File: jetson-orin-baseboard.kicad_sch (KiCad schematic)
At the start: 4 parts

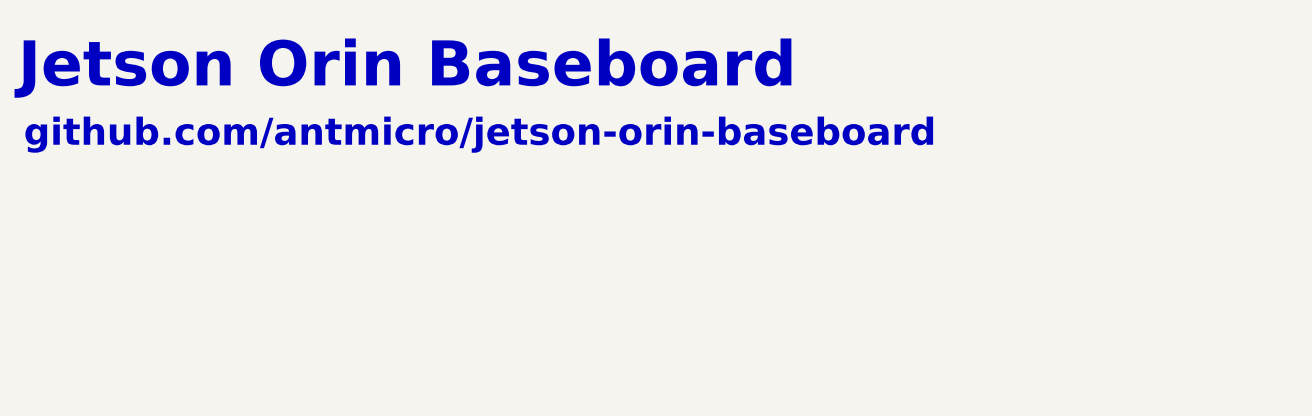
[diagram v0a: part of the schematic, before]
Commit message: PCIE Simplification finished
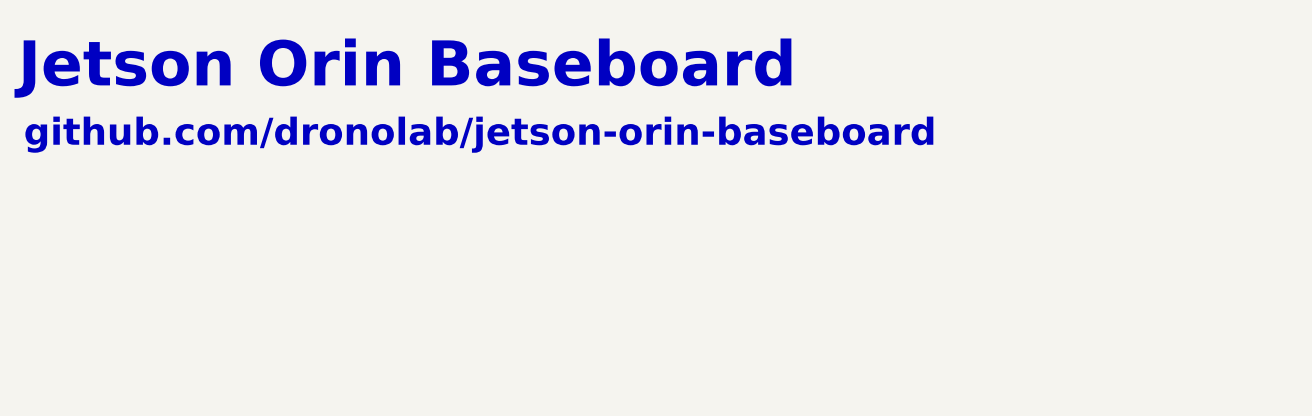
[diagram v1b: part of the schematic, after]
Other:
- note added: "github.com/dronolab/jetson-orin-baseboard"
- note removed: "github.com/antmicro/jetson-orin-baseboard"
- company: Antmicro Ltd -> Dronolab

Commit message: Simplification continues
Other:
- removed sheet HDMI

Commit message: Added things left to do list
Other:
- note added: "Merge usb-c debug et usb-c 1(sheet usb3) Ajouter buzzer, imu, microphone Choisir une camera(déterminer les critères qu'on désire)(Voir pour stéréo déjà faite ou qu'on fait nous même) Quand on va avoir une camera : Changer les CSI/interface en fonction du protocole de la camera choisie Ajouter la 4G Ajouter un port ARA juste le Jetson carrier board(16 pin du ARA sur 16 pin qui arrive sur le Jetson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"
- note added: "THINGS LEFT TO DO"
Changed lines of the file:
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@@
     (effects (font (size 3 3) (thickness 0.4) bold) (justify left bottom))
+  )
+  (text "THINGS LEFT TO DO" (at 151.765 45.72 0)
+    (effects (font (size 8 8) (thickness 0.3) bold) (justify left bottom))
+  )
+  (text "Merge usb-c debug et usb-c 1(sheet usb3)\nAjouter buzzer, imu, microphone\nChoisir une camera(déterminer les critères qu'on désire)(Voir pour stéréo déjà faite ou qu'on fait nous même)\nQuand on va avoir une camera : Changer les CSI/interface en fonction du protocole de la camera choisie\nAjouter la 4G\nAjouter un port ARA juste le Jetson carrier board(16 pin du ARA sur 16 pin qui arrive sur le Jetson)\nRefaire le connecteur PAC(Expansion Connector)"
+    (at 155.575 64.135 0)
+    (effects (font (size 1.27 1.27)) (justify left bottom))
   )
   (text "Jetson Orin Baseboard" (at 13.97 24.765 0)

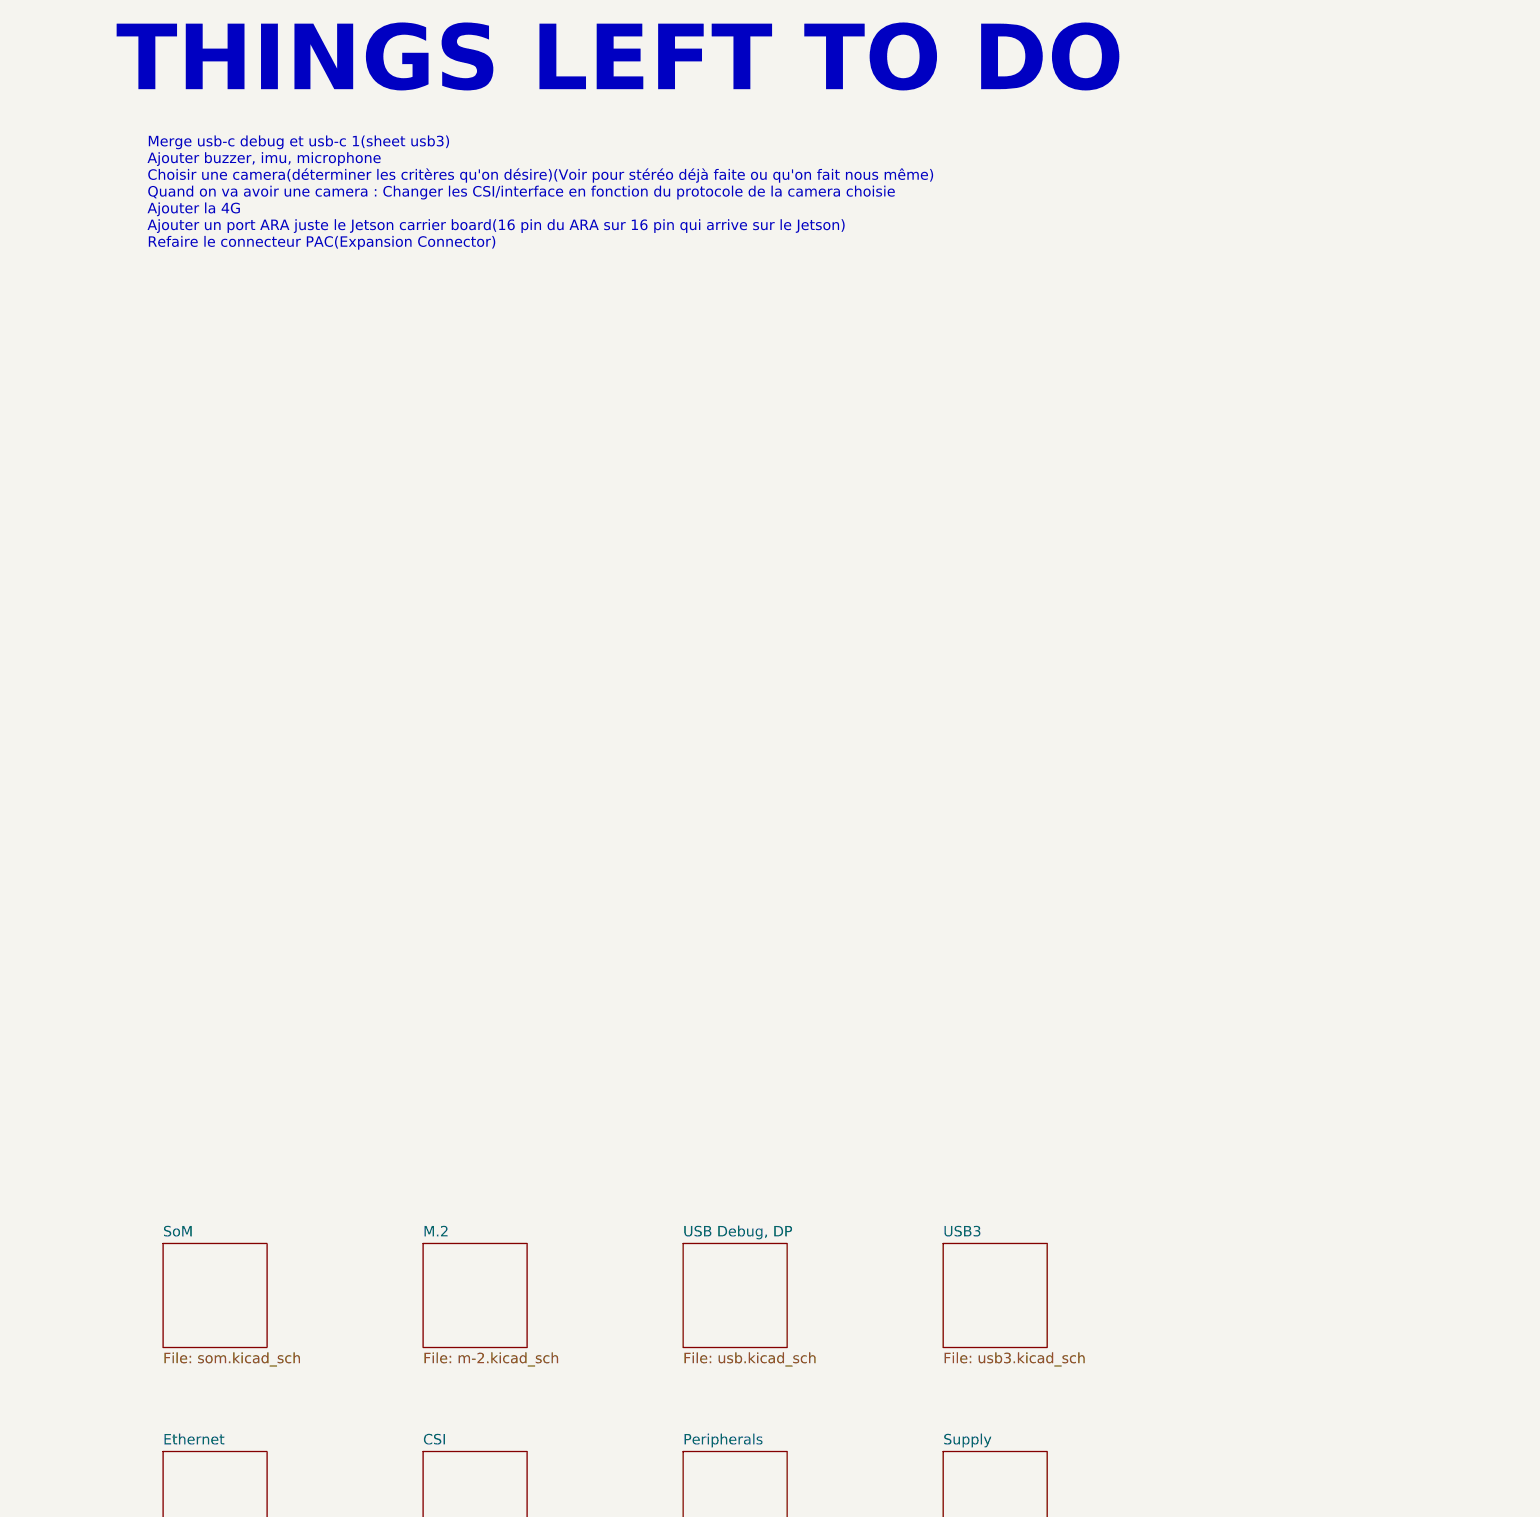
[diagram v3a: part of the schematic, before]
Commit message: Added IMU + MICROPHONES
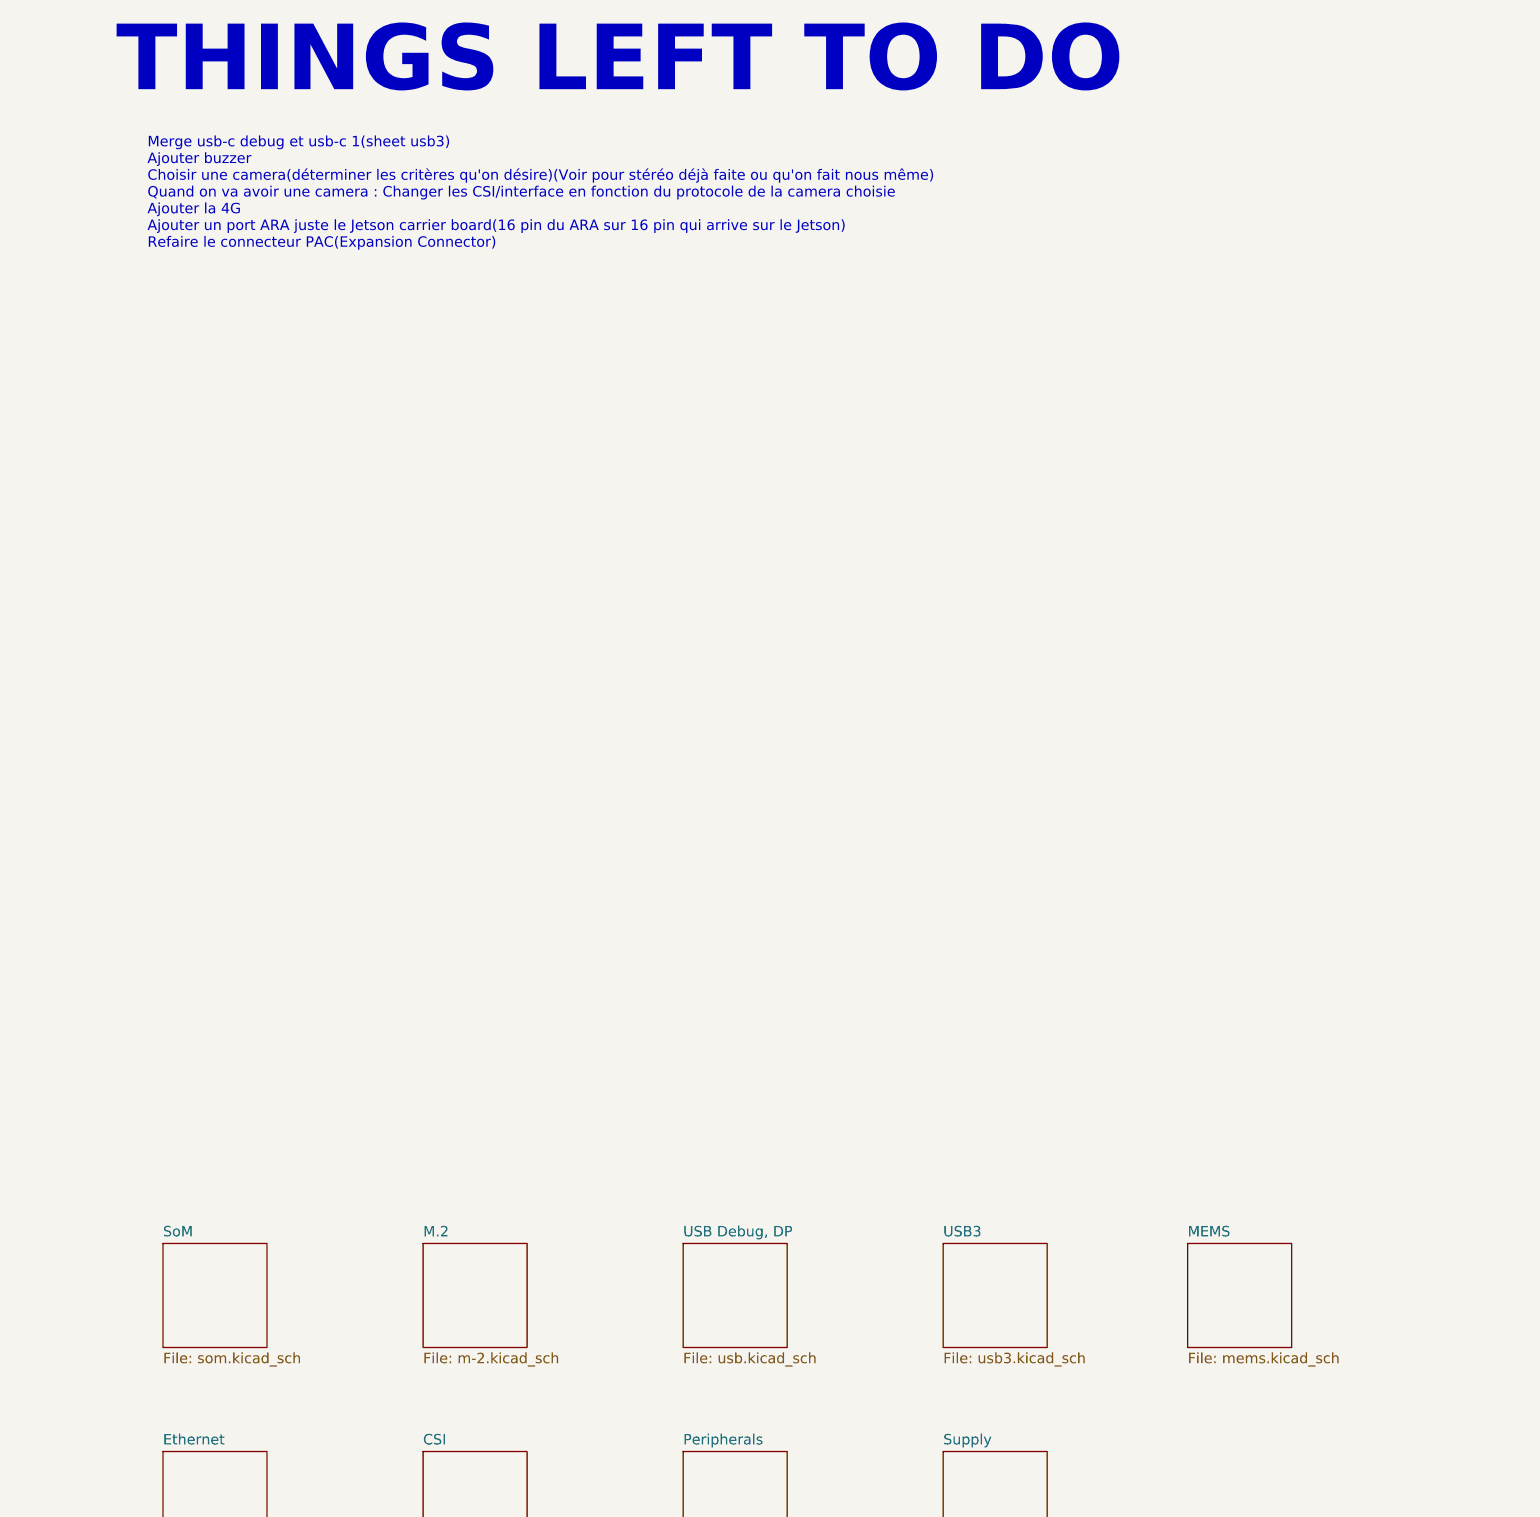
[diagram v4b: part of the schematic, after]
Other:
- added sheet MEMS (mems.kicad_sch)
- note added: "Merge usb-c debug et usb-c 1(sheet usb3) Ajouter buzzer Choisir une camera(déterminer les critères qu'on désire)(Voir pour stéréo déjà faite ou qu'on fait nous même) Quand on va avoir une camera : Changer les CSI/interface en fonction du protocole de la camera choisie Ajouter la 4G Ajouter un port ARA juste le Jetson carrier board(16 pin du ARA sur 16 pin qui arrive sur le Jetson) Refaire le conn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"
- note removed: "Merge usb-c debug et usb-c 1(sheet usb3) Ajouter buzzer, imu, microphone Choisir une camera(déterminer les critères qu'on désire)(Voir pour stéréo déjà faite ou qu'on fait nous même) Quand on va avoir une camera : Changer les CSI/interface en fonction du protocole de la camera choisie Ajouter la 4G Ajouter un port ARA juste le Jetson carrier board(16 pin du ARA sur 16 pin qui arrive sur le Jetson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"
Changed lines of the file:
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@@
   (title_block
     (title "Jetson Orin Baseboard")
-    (date "2023-07-05")
+    (date "2023-07-09")
     (rev "1.0.0")
     (company "Dronolab")
@@
     (effects (font (size 8 8) (thickness 0.3) bold) (justify left bottom))
   )
-  (text "Merge usb-c debug et usb-c 1(sheet usb3)\nAjouter buzzer, imu, microphone\nChoisir une camera(déterminer les critères qu'on désire)(Voir pour stéréo déjà faite ou qu'on fait nous même)\nQuand on va avoir une camera : Changer les CSI/interface en fonction du protocole de la camera choisie\nAjouter la 4G\nAjouter un port ARA juste le Jetson carrier board(16 pin du ARA sur 16 pin qui arrive sur le Jetson)\nRefaire le connecteur PAC(Expansion Connector)"
+  (text "Merge usb-c debug et usb-c 1(sheet usb3)\nAjouter buzzer\nChoisir une camera(déterminer les critères qu'on désire)(Voir pour stéréo déjà faite ou qu'on fait nous même)\nQuand on va avoir une camera : Changer les CSI/interface en fonction du protocole de la camera choisie\nAjouter la 4G\nAjouter un port ARA juste le Jetson carrier board(16 pin du ARA sur 16 pin qui arrive sur le Jetson)\nRefaire le connecteur PAC(Expansion Connector)"
     (at 155.575 64.135 0)
     (effects (font (size 1.27 1.27)) (justify left bottom))
@@
       )
     )
+  )
+  (sheet (at 282.575 185.42) (size 12.7 12.7) (fields_autoplaced)
+    (stroke (width 0.1524) (type solid))
+    (fill (color 0 0 0 0.0000))
+    (property "Sheetname" "MEMS" (at 282.575 184.7084 0)
+      (effects (font (size 1.27 1.27)) (justify left bottom))
+    )
+    (property "Sheetfile" "mems.kicad_sch" (at 282.575 198.7046 0)
+      (effects (font (size 1.27 1.27)) (justify left top))
+    )
+    (instances
+      (project "jetson-orin-baseboard"
+        (path "/4b393452-b11e-416e-bc83-918ae3cab2f1" (page "10"))
+      )
+    )

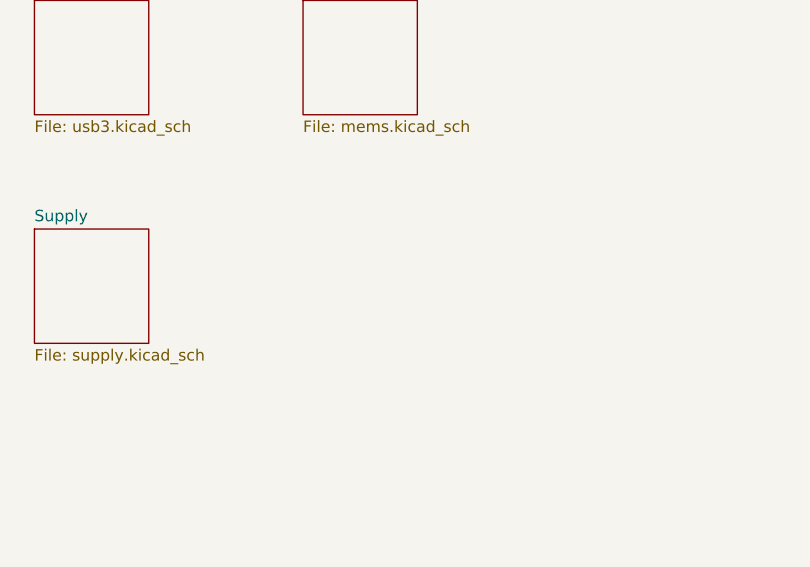
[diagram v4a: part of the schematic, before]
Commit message: Add 4G Sheet
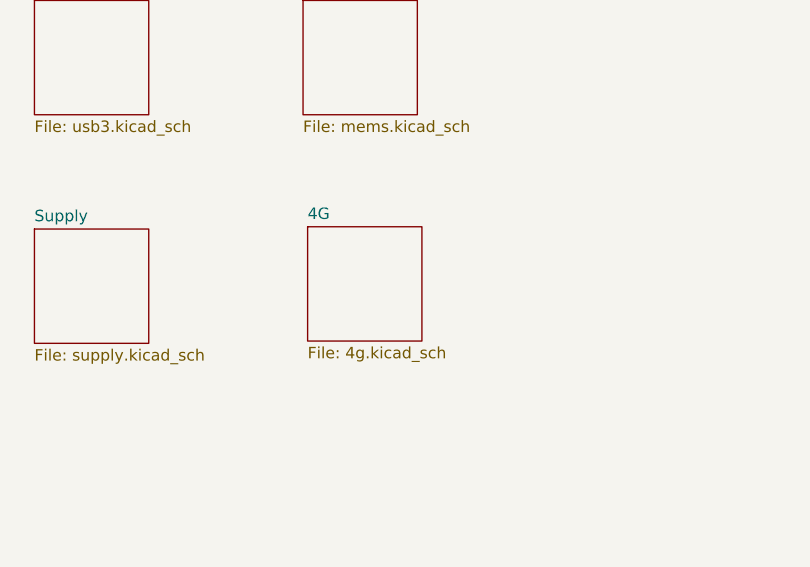
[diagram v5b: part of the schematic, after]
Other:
- added sheet 4G (4g.kicad_sch)
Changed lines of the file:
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@@
+    )
+  )
+  (sheet (at 283.083 210.566) (size 12.7 12.7) (fields_autoplaced)
+    (stroke (width 0.1524) (type solid))
+    (fill (color 0 0 0 0.0000))
+    (property "Sheetname" "4G" (at 283.083 209.8544 0)
+      (effects (font (size 1.27 1.27)) (justify left bottom))
+    )
+    (property "Sheetfile" "4g.kicad_sch" (at 283.083 223.8506 0)
+      (effects (font (size 1.27 1.27)) (justify left top))
+    )
+    (instances
+      (project "jetson-orin-baseboard"
+        (path "/4b393452-b11e-416e-bc83-918ae3cab2f1" (page "11"))
+      )
     )
   )
